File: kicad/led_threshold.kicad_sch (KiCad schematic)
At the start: 16 parts, among them Q1 2N7002E, Q2 2N7002E, SW5 EG6100-ND, U21 OPA189, U22 4x Comparator

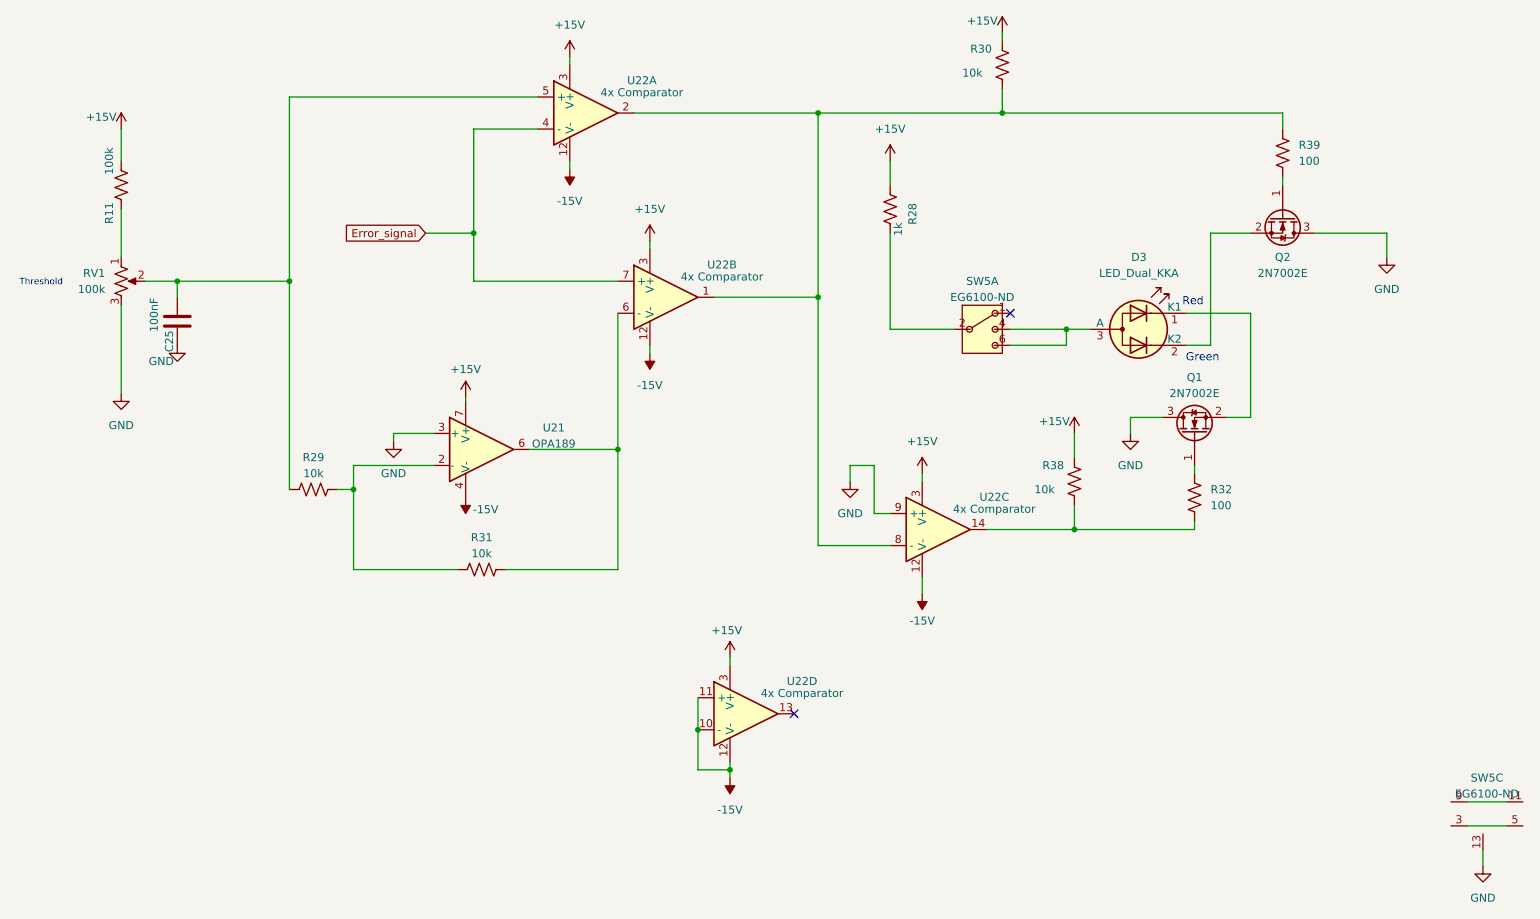
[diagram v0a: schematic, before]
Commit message: Updated Design, more compact layout, precise location values for I/O, Fixed TrimPot footprint, TODO: Finalize BOM, add partnos for SMD R/Cs
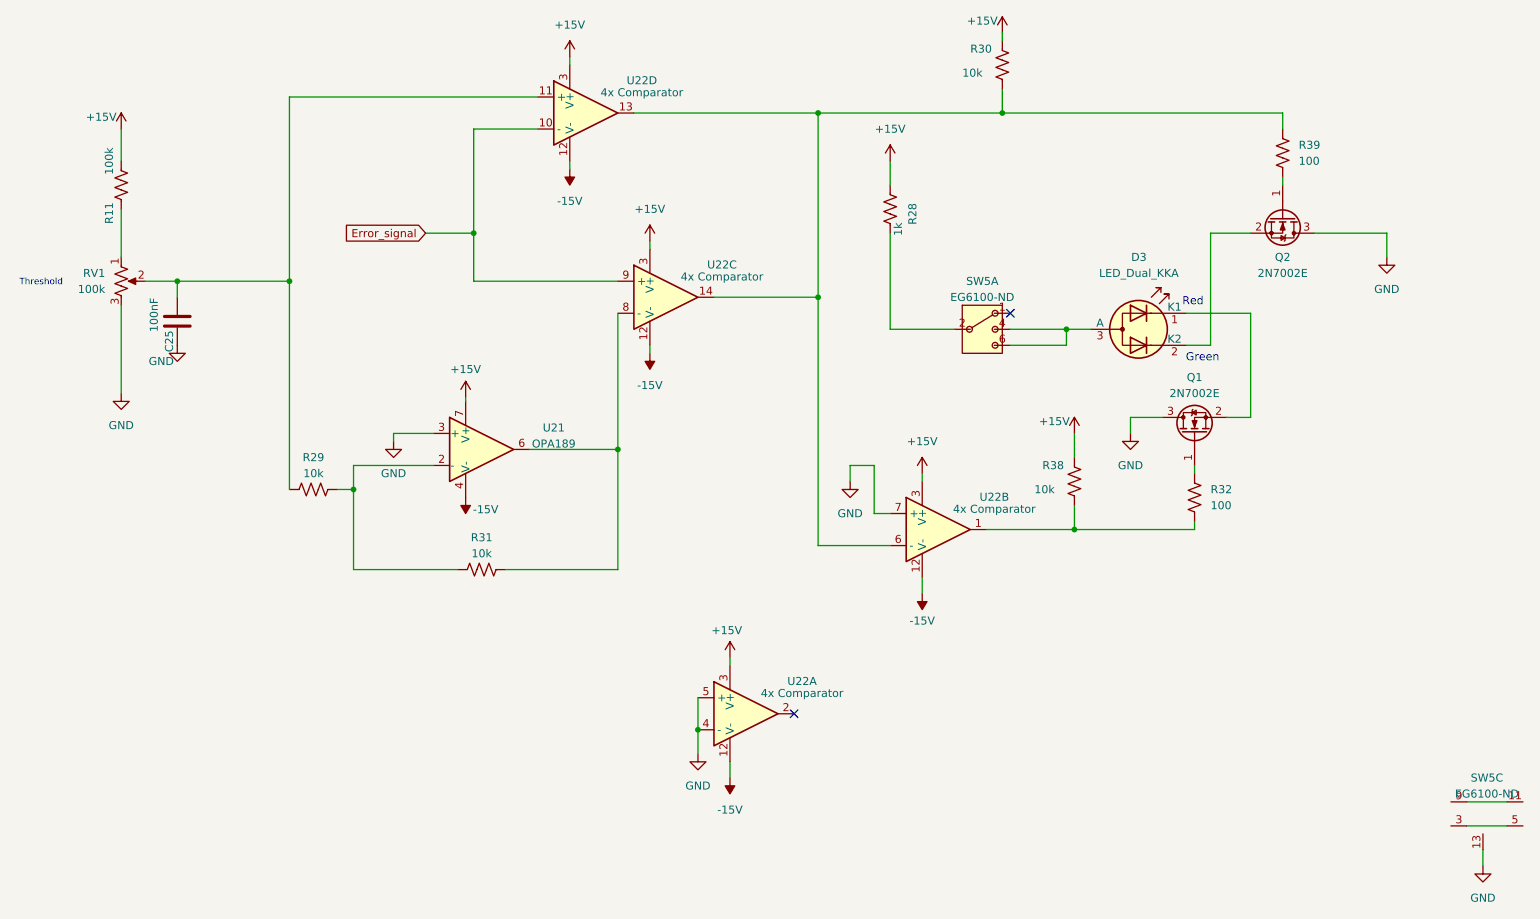
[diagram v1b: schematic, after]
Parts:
- RV1: footprint Connector_PinHeader_2.54mm:PinHeader_1x03_P2.54mm_Vertical -> Potentiometer_THT:Potentiometer_Bourns_3296W_Vertical
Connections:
- net -15V: no longer U22.10 (-), U22.11 (+)
- net Error_signal: now also U22.10 (-), U22.9 (+); no longer U22.4 (-), U22.7 (+)
- net GND: now also U22.4 (-), U22.5 (+), U22.7 (+); no longer U22.9 (+)
- net at R32.2, R38.1: now also U22.1; no longer U22.14
- net at C25.2, R29.1, RV1.2: now also U22.11 (+); no longer U22.5 (+)
- net at R31.2, U21.6: now also U22.8 (-); no longer U22.6 (-)
- net at U22.13: now also R30.1, R39.1, U22.14, U22.6 (-)
- now unconnected: U22.2
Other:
- moved on the sheet: U22A, U22B, U22C, U22D
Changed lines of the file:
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@@
 	)
 	(junction
-		(at 140.97 135.89)
-		(diameter 0)
-		(color 0 0 0 0)
-	)
-	(junction
 		(at 135.89 129.54)
 		(diameter 0)
@@
 	(wire
 		(pts
-			(xy 135.89 135.89) (xy 140.97 135.89)
-		)
-		(stroke
-			(width 0)
-			(type default)
-		)
-	)
-	(wire
-		(pts
-			(xy 135.89 129.54) (xy 135.89 135.89)
-		)
-		(stroke
-			(width 0)
-			(type default)
-		)
-	)
-	(wire
-		(pts
 			(xy 213.36 63.5) (xy 223.52 63.5)
 		)
@@
 	(wire
 		(pts
+			(xy 135.89 129.54) (xy 135.89 133.35)
+		)
+		(stroke
+			(width 0)
+			(type default)
+		)
+	)
+	(wire
+		(pts
 			(xy 160.02 87.63) (xy 160.02 90.17)
 		)
@@
 	(wire
 		(pts
-			(xy 140.97 137.16) (xy 140.97 135.89)
+			(xy 140.97 134.62) (xy 140.97 137.16)
 		)
 		(stroke
@@
 	(wire
 		(pts
-			(xy 140.97 135.89) (xy 140.97 134.62)
-		)
-		(stroke
-			(width 0)
-			(type default)
-		)
-	)
-	(wire
-		(pts
 			(xy 105.41 104.14) (xy 123.19 104.14)
 		)
@@
 	(symbol
 		(lib_id "Custom_Symbols:Quad Comparator")
-		(at 129.54 60.96 0)
+		(at 172.72 97.79 0)
 		(unit 2)
 		(exclude_from_sim no)
@@
 		(fields_autoplaced yes)
 		(property "Reference" "U22"
-			(at 139.7 55.8098 0)
+			(at 182.88 92.6398 0)
 			(effects
 				(font
@@
 		)
 		(property "Value" "4x Comparator"
-			(at 139.7 57.7149 0)
+			(at 182.88 94.5449 0)
 			(effects
 				(font
@@
 		)
 		(property "Footprint" "Custom_Footprints:SOIC-14"
-			(at 129.54 60.96 0)
+			(at 172.72 97.79 0)
 			(effects
 				(font
@@
 		)
 		(property "Datasheet" ""
-			(at 129.54 60.96 0)
+			(at 172.72 97.79 0)
 			(effects
 				(font
@@
 		)
 		(property "Description" ""
-			(at 129.54 60.96 0)
+			(at 172.72 97.79 0)
 			(effects
 				(font
@@
 		)
 		(property "DIGIKEY" "UPC177G2(20)-E2-A"
-			(at 129.54 60.96 0)
+			(at 172.72 97.79 0)
 			(effects
 				(font
@@
 		)
 		(property "MOUSER" "968-UPC177G220-E2A"
-			(at 129.54 60.96 0)
+			(at 172.72 97.79 0)
 			(effects
 				(font
@@
 		)
 		(property "PARTNO" "UPC177G2(20)-E2-A"
-			(at 129.54 60.96 0)
+			(at 172.72 97.79 0)
 			(effects
 				(font
@@
 		)
 		(property "MPN" ""
-			(at 129.54 60.96 0)
+			(at 172.72 97.79 0)
 			(effects
 				(font
@@
 	)
 	(symbol
+		(lib_name "GND_5")
+		(lib_id "power:GND")
+		(at 135.89 133.35 0)
+		(unit 1)
+		(exclude_from_sim no)
+		(in_bom yes)
+		(on_board yes)
+		(dnp no)
+		(fields_autoplaced yes)
+		(property "Reference" "#PWR040"
+			(at 135.89 139.7 0)
+			(effects
+				(font
+					(size 1.27 1.27)
+				)
+				(hide yes)
+			)
+		)
+		(property "Value" "GND"
+			(at 135.89 138.43 0)
+			(effects
+				(font
+					(size 1.27 1.27)
+				)
+			)
+		)
+		(property "Footprint" ""
+			(at 135.89 133.35 0)
+			(effects
+				(font
+					(size 1.27 1.27)
+				)
+				(hide yes)
+			)
+		)
+		(property "Datasheet" ""
+			(at 135.89 133.35 0)
+			(effects
+				(font
+					(size 1.27 1.27)
+				)
+				(hide yes)
+			)
+		)
+		(property "Description" "Power symbol creates a global label with name \"GND\" , ground"
+			(at 135.89 133.35 0)
+			(effects
+				(font
+					(size 1.27 1.27)
+				)
+				(hide yes)
+			)
+		)
+		(pin "1"
+		)
+		(instances
+			(project ""
+				(path "/3a3d7bcb-6fa5-41ef-9ea1-6d4ab7c492fd/0e4e37c0-2fc7-4de2-ba74-9d178da3762c"
+					(reference "#PWR040")
+					(unit 1)
+				)
+			)
+		)
+	)
+	(symbol
 		(lib_id "power:-15V")
 		(at 99.06 92.71 180)
@@
 	(symbol
 		(lib_id "Custom_Symbols:Quad Comparator")
-		(at 172.72 97.79 0)
+		(at 129.54 60.96 0)
 		(unit 3)
 		(exclude_from_sim no)
@@
 		(fields_autoplaced yes)
 		(property "Reference" "U22"
-			(at 182.88 92.6398 0)
+			(at 139.7 55.8098 0)
 			(effects
 				(font
@@
 		)
 		(property "Value" "4x Comparator"
-			(at 182.88 94.5449 0)
+			(at 139.7 57.7149 0)
 			(effects
 				(font
@@
 		)
 		(property "Footprint" "Custom_Footprints:SOIC-14"
-			(at 172.72 97.79 0)
+			(at 129.54 60.96 0)
 			(effects
 				(font
@@
 		)
 		(property "Datasheet" ""
-			(at 172.72 97.79 0)
+			(at 129.54 60.96 0)
 			(effects
 				(font
@@
 		)
 		(property "Description" ""
-			(at 172.72 97.79 0)
+			(at 129.54 60.96 0)
 			(effects
 				(font
@@
 		)
 		(property "DIGIKEY" "UPC177G2(20)-E2-A"
-			(at 172.72 97.79 0)
+			(at 129.54 60.96 0)
 			(effects
 				(font
@@
 		)
 		(property "MOUSER" "968-UPC177G220-E2A"
-			(at 172.72 97.79 0)
+			(at 129.54 60.96 0)
 			(effects
 				(font
@@
 		)
 		(property "PARTNO" "UPC177G2(20)-E2-A"
-			(at 172.72 97.79 0)
+			(at 129.54 60.96 0)
 			(effects
 				(font
@@
 		)
 		(property "MPN" ""
-			(at 172.72 97.79 0)
+			(at 129.54 60.96 0)
 			(effects
 				(font
@@
 			)
 		)
-		(property "Footprint" "Connector_PinHeader_2.54mm:PinHeader_1x03_P2.54mm_Vertical"
+		(property "Footprint" "Potentiometer_THT:Potentiometer_Bourns_3296W_Vertical"
 			(at 44.45 58.42 0)
 			(effects
@@
 	(symbol
 		(lib_id "Custom_Symbols:Quad Comparator")
-		(at 142.24 127 0)
+		(at 116.84 31.75 0)
 		(unit 4)
 		(exclude_from_sim no)
@@
 		(fields_autoplaced yes)
 		(property "Reference" "U22"
-			(at 152.4 121.8498 0)
+			(at 127 26.5998 0)
 			(effects
 				(font
@@
 		)
 		(property "Value" "4x Comparator"
-			(at 152.4 123.7549 0)
+			(at 127 28.5049 0)
 			(effects
 				(font
@@
 		)
 		(property "Footprint" "Custom_Footprints:SOIC-14"
-			(at 142.24 127 0)
+			(at 116.84 31.75 0)
 			(effects
 				(font
@@
 		)
 		(property "Datasheet" ""
-			(at 142.24 127 0)
+			(at 116.84 31.75 0)
 			(effects
 				(font
@@
 		)
 		(property "Description" ""
-			(at 142.24 127 0)
+			(at 116.84 31.75 0)
 			(effects
 				(font
@@
 		)
 		(property "DIGIKEY" "UPC177G2(20)-E2-A"
-			(at 142.24 127 0)
+			(at 116.84 31.75 0)
 			(effects
 				(font
@@
 		)
 		(property "MOUSER" "968-UPC177G220-E2A"
-			(at 142.24 127 0)
+			(at 116.84 31.75 0)
 			(effects
 				(font
@@
 		)
 		(property "PARTNO" "UPC177G2(20)-E2-A"
-			(at 142.24 127 0)
+			(at 116.84 31.75 0)
 			(effects
 				(font
@@
 		)
 		(property "MPN" ""
-			(at 142.24 127 0)
+			(at 116.84 31.75 0)
 			(effects
 				(font
@@
 	(symbol
 		(lib_id "Custom_Symbols:Quad Comparator")
-		(at 116.84 31.75 0)
+		(at 142.24 127 0)
 		(unit 1)
 		(exclude_from_sim no)
@@
 		(fields_autoplaced yes)
 		(property "Reference" "U22"
-			(at 127 26.5998 0)
+			(at 152.4 121.8498 0)
 			(effects
 				(font
@@
 		)
 		(property "Value" "4x Comparator"
-			(at 127 28.5049 0)
+			(at 152.4 123.7549 0)
 			(effects
 				(font
@@
 		)
 		(property "Footprint" "Custom_Footprints:SOIC-14"
-			(at 116.84 31.75 0)
+			(at 142.24 127 0)
 			(effects
 				(font
@@
 		)
 		(property "Datasheet" ""
-			(at 116.84 31.75 0)
+			(at 142.24 127 0)
 			(effects
 				(font
@@
 		)
 		(property "Description" ""
-			(at 116.84 31.75 0)
+			(at 142.24 127 0)
 			(effects
 				(font
@@
 		)
 		(property "DIGIKEY" "UPC177G2(20)-E2-A"
-			(at 116.84 31.75 0)
+			(at 142.24 127 0)
 			(effects
 				(font
@@
 		)
 		(property "MOUSER" "968-UPC177G220-E2A"
-			(at 116.84 31.75 0)
+			(at 142.24 127 0)
 			(effects
 				(font
@@
 		)
 		(property "PARTNO" "UPC177G2(20)-E2-A"
-			(at 116.84 31.75 0)
+			(at 142.24 127 0)
 			(effects
 				(font
@@
 		)
 		(property "MPN" ""
-			(at 116.84 31.75 0)
+			(at 142.24 127 0)
 			(effects
 				(font

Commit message: Minor Layout updates, replaced old component part no's, added part no's for rest of parts
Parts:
- C25: DIGIKEY (none) -> 1276-6840-2-ND; PARTNO (none) -> CL21B104KCFNNNE
- R11: DIGIKEY (none) -> P100KDATR-ND; PARTNO (none) -> ERA-6AEB104V
- R28: DIGIKEY (none) -> 5831-2-2176327-5TR-ND; PARTNO (none) -> 2-2176327-5
- R29, R30, R31, R38: PARTNO (none) -> RN73H2ATTD1002B25
- R32, R39: DIGIKEY (none) -> P16057TR-ND; PARTNO (none) -> ERJ-P06F1000V
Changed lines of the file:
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@@
+			)
+		)
+		(property "PARTNO" "RN73H2ATTD1002B25"
+			(at 195.58 90.17 0)
+			(effects
+				(font
+					(size 1.27 1.27)
+				)
+				(hide yes)
 			)
 		)
@@
 			)
 		)
+		(property "PARTNO" "RN73H2ATTD1002B25"
+			(at 74.93 91.44 90)
+			(effects
+				(font
+					(size 1.27 1.27)
+				)
+				(hide yes)
+			)
+		)
 		(pin "1"
 		)
@@
 			)
 		)
+		(property "PARTNO" "RN73H2ATTD1002B25"
+			(at 184.15 24.13 0)
+			(effects
+				(font
+					(size 1.27 1.27)
+				)
+				(hide yes)
+			)
+		)
 		(pin "1"
 		)
@@
 			)
 		)
-		(property "DIGIKEY" ""
+		(property "DIGIKEY" "P100KDATR-ND"
 			(at 44.45 43.18 0)
 			(effects
@@
 		)
 		(property "MPN" ""
+			(at 44.45 43.18 90)
+			(effects
+				(font
+					(size 1.27 1.27)
+				)
+				(hide yes)
+			)
+		)
+		(property "PARTNO" "ERA-6AEB104V"
 			(at 44.45 43.18 90)
 			(effects
@@
 			)
 		)
+		(property "PARTNO" "RN73H2ATTD1002B25"
+			(at 101.6 104.14 90)
+			(effects
+				(font
+					(size 1.27 1.27)
+				)
+				(hide yes)
+			)
+		)
 		(pin "1"
 		)
@@
 			)
 		)
+		(property "DIGIKEY" "P16057TR-ND"
+			(at 228.6 38.1 0)
+			(effects
+				(font
+					(size 1.27 1.27)
+				)
+				(hide yes)
+			)
+		)
+		(property "PARTNO" "ERJ-P06F1000V"
+			(at 228.6 38.1 0)
+			(effects
+				(font
+					(size 1.27 1.27)
+				)
+				(hide yes)
+			)
+		)
 		(pin "1"
 		)
@@
 			)
 		)
+		(property "DIGIKEY" "P16057TR-ND"
+			(at 214.63 92.71 0)
+			(effects
+				(font
+					(size 1.27 1.27)
+				)
+				(hide yes)
+			)
+		)
+		(property "PARTNO" "ERJ-P06F1000V"
+			(at 214.63 92.71 0)
+			(effects
+				(font
+					(size 1.27 1.27)
+				)
+				(hide yes)
+			)
+		)
 		(pin "1"
 		)
@@
 			)
 		)
-		(property "DIGIKEY" ""
+		(property "DIGIKEY" "5831-2-2176327-5TR-ND"
 			(at 166.37 46.99 90)
 			(effects
@@
 			)
 		)
-		(property "PARTNO" ""
+		(property "PARTNO" "2-2176327-5"
 			(at 166.37 46.99 90)
 			(effects
@@
 			(at 53.34 64.77 90)
 			(effects
+				(font
+					(size 1.27 1.27)
+				)
+				(hide yes)
+			)
+		)
+		(property "DIGIKEY" "1276-6840-2-ND "
+			(at 53.34 64.77 90)
+			(effects
+				(font
+					(size 1.27 1.27)
+				)
+				(hide yes)
+			)
+		)
+		(property "PARTNO" "CL21B104KCFNNNE"
+			(at 53.34 64.77 90)
+			(effects

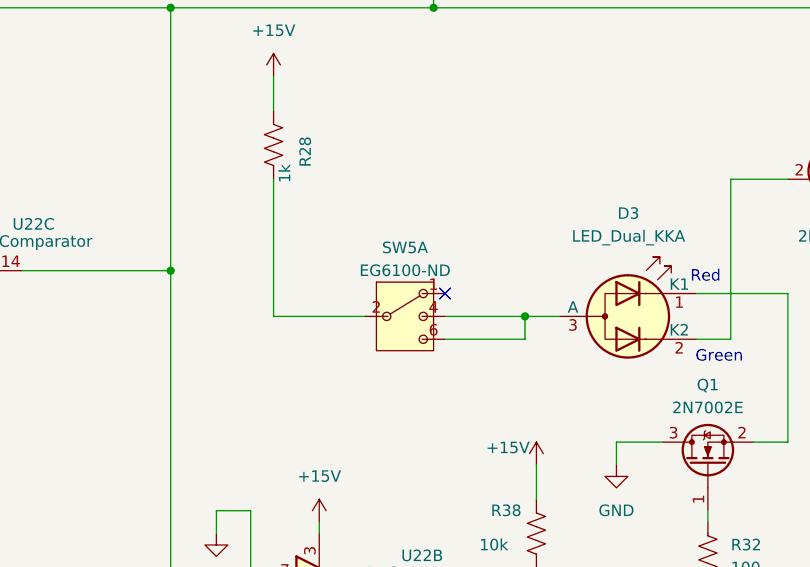
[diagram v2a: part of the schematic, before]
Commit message: Connected other leg of Pots, added 3d models from manufacturer for switch+pots
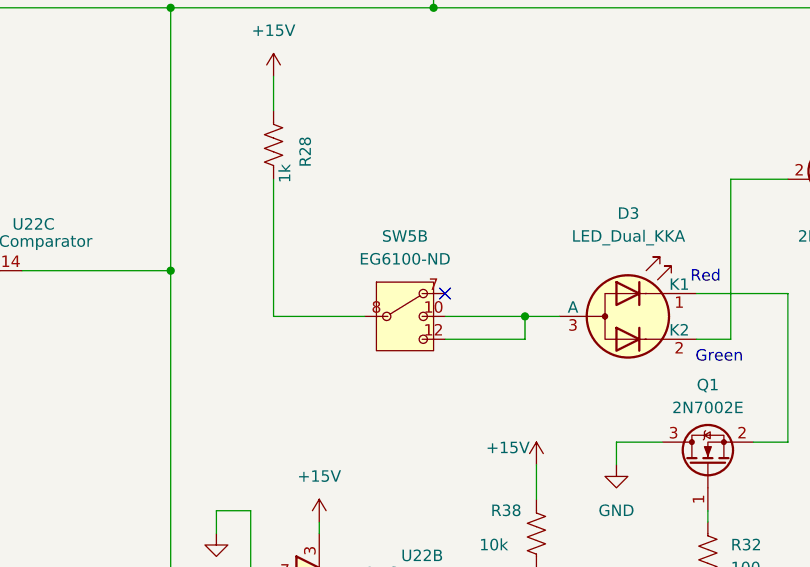
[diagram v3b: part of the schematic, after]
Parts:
- removed unit 1 of SW5
- added unit 2 of SW5
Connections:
- net at R28.2: now also SW5.8
- net at D3.3 (A): now also SW5.10, SW5.12
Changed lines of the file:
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@@
+	)
+	(symbol
+		(lib_id "Custom_Symbols:DP3T_1")
+		(at 180.34 66.04 0)
+		(unit 2)
+		(exclude_from_sim no)
+		(in_bom yes)
+		(on_board yes)
+		(dnp no)
+		(fields_autoplaced yes)
+		(property "Reference" "SW5"
+			(at 180.975 57.15 0)
+			(effects
+				(font
+					(size 1.27 1.27)
+				)
+			)
+		)
+		(property "Value" "EG6100-ND"
+			(at 180.975 59.69 0)
+			(effects
+				(font
+					(size 1.27 1.27)
+				)
+			)
+		)
+		(property "Footprint" "Custom_Footprints:Right Angle 3PDT Switch"
+			(at 180.34 66.04 0)
+			(effects
+				(font
+					(size 1.27 1.27)
+				)
+				(hide yes)
+			)
+		)
+		(property "Datasheet" ""
+			(at 180.34 66.04 0)
+			(effects
+				(font
+					(size 1.27 1.27)
+				)
+				(hide yes)
+			)
+		)
+		(property "Description" ""
+			(at 180.34 66.04 0)
+			(effects
+				(font
+					(size 1.27 1.27)
+				)
+				(hide yes)
+			)
+		)
+		(property "DIGIKEY" "EG6100-ND"
+			(at 180.34 66.04 0)
+			(effects
+				(font
+					(size 1.27 1.27)
+				)
+				(hide yes)
+			)
+		)
+		(property "PARTNO" "1004P6T1B4M7RE"
+			(at 180.34 66.04 0)
+			(effects
+				(font
+					(size 1.27 1.27)
+				)
+				(hide yes)
+			)
+		)
+		(property "MPN" ""
+			(at 180.34 66.04 0)
+			(effects
+				(font
+					(size 1.27 1.27)
+				)
+				(hide yes)
+			)
+		)
+		(pin "9"
+		)
+		(pin "10"
+		)
+		(pin "3"
+		)
+		(pin "5"
+		)
+		(pin "12"
+		)
+		(pin "8"
+		)
+		(pin "11"
+		)
+		(pin "7"
+		)
+		(pin "13"
+		)
+		(pin "6"
+		)
+		(pin "2"
+		)
+		(pin "4"
+		)
+		(pin "1"
+		)
+		(instances
+			(project "intensity_pi"
+				(path "/3a3d7bcb-6fa5-41ef-9ea1-6d4ab7c492fd/0e4e37c0-2fc7-4de2-ba74-9d178da3762c"
+					(reference "SW5")
+					(unit 2)
+				)
+			)
+		)
 	)
 	(symbol
@@
 					(unit 1)
 				)
-			)
-		)
-	)
-	(symbol
-		(lib_id "Custom_Symbols:DP3T_1")
-		(at 180.34 66.04 0)
-		(unit 1)
-		(exclude_from_sim no)
-		(in_bom yes)
-		(on_board yes)
-		(dnp no)
-		(fields_autoplaced yes)
-		(property "Reference" "SW5"
-			(at 180.975 58.42 0)
-			(effects
-				(font
-					(size 1.27 1.27)
-				)
-			)
-		)
-		(property "Value" "EG6100-ND"
-			(at 180.975 60.96 0)
-			(effects
-				(font
-					(size 1.27 1.27)
-				)
-			)
-		)
-		(property "Footprint" "Custom_Footprints:Right Angle 3PDT Switch"
-			(at 180.34 66.04 0)
-			(effects
-				(font
-					(size 1.27 1.27)
-				)
-				(hide yes)
-			)
-		)
-		(property "Datasheet" ""
-			(at 180.34 66.04 0)
-			(effects
-				(font
-					(size 1.27 1.27)
-				)
-				(hide yes)
-			)
-		)
-		(property "Description" ""
-			(at 180.34 66.04 0)
-			(effects
-				(font
-					(size 1.27 1.27)
-				)
-				(hide yes)
-			)
-		)
-		(property "DIGIKEY" "EG6100-ND"
-			(at 180.34 66.04 0)
-			(effects
-				(font
-					(size 1.27 1.27)
-				)
-				(hide yes)
-			)
-		)
-		(property "PARTNO" "1004P6T1B4M7RE"
-			(at 180.34 66.04 0)
-			(effects
-				(font
-					(size 1.27 1.27)
-				)
-				(hide yes)
-			)
-		)
-		(property "MPN" ""
-			(at 180.34 66.04 0)
-			(effects
-				(font
-					(size 1.27 1.27)
-				)
-				(hide yes)
-			)
-		)
-		(pin "9"
-		)
-		(pin "10"
-		)
-		(pin "3"
-		)
-		(pin "5"
-		)
-		(pin "12"
-		)
-		(pin "8"
-		)
-		(pin "11"
-		)
-		(pin "7"
-		)
-		(pin "13"
-		)
-		(pin "6"
-		)
-		(pin "2"
-		)
-		(pin "4"
-		)
-		(pin "1"
-		)
-		(instances
-			(project "intensity_pi"
-				(path "/3a3d7bcb-6fa5-41ef-9ea1-6d4ab7c492fd/0e4e37c0-2fc7-4de2-ba74-9d178da3762c"
-					(reference "SW5")
-					(unit 1)
-				)
